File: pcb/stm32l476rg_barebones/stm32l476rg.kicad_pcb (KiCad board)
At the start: 4 copper layers, 50 x 38 mm, 49 parts, among them J1 Conn_01x04_UART, J2 Conn_01x04_I2C, J3 Conn_01x06_SPI, J4 SWD_Connector, J5 USB_B_Micro, J6 Screw_Terminal_01x02, Q1 AO3401A, SW1 SW_SPDT, U1 USBLC6-2SC6, U2 MP2359DJ-LF-Z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

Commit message: Pre barebones route
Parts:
- moved R8 3.26 mm to (143.3, 129.9), turned to 90 degrees
- moved D1 1.57 mm to (144.0, 114.2)
- moved U1 1.44 mm to (140.3, 113.8)
- moved R6 0.80 mm to (140.0, 129.9)
- moved R7 0.80 mm to (141.7, 129.9)
- moved Q1 0.55 mm to (143.2, 122.4)
- moved J6 0.35 mm to (149.2, 124.4)
- moved D3 0.30 mm to (147.5, 130.0)
- moved L2 0.27 mm to (133.2, 127.7)
- moved C7 0.25 mm to (137.1, 126.0)
- moved D2 0.25 mm to (133.7, 123.0)
- moved D4 0.14 mm to (147.5, 117.5)
- moved R11 0.14 mm to (147.5, 115.5)
- moved R10 0.10 mm to (147.5, 128.0)
- turned J5 to 180 degrees
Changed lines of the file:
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@@
   )
   (module Capacitor_SMD:C_0603_1608Metric (layer F.Cu)
-    (at 136.8 125.9 270)
+    (at 137.05 125.95 270)
     (descr "Capacitor SMD 0603 (1608 Metric), square (rectangular) end terminal, IPC_7351 nominal, (Body size source: IPC-SM-782 page 76, https://www.pcb-3d.com/wordpress/wp-content/uploads/ipc-sm-782a_amendment_1_and_2.pdf), generated with kicad-footprint-generator")
     (tags capacitor)
@@
   )
   (module Diode_SMD:D_SOD-123 (layer F.Cu)
-    (at 142.5 114.7 90)
+    (at 144 114.25 90)
     (descr SOD-123)
     (tags SOD-123)
@@
   )
   (module Diode_SMD:D_SOD-123 (layer F.Cu)
-    (at 133.4 123 180)
+    (at 133.65 123 180)
     (descr SOD-123)
     (tags SOD-123)
@@
   )
   (module LED_SMD:LED_0603_1608Metric (layer F.Cu)
-    (at 147.5 129.7 180)
+    (at 147.5 130 180)
     (descr "LED SMD 0603 (1608 Metric), square (rectangular) end terminal, IPC_7351 nominal, (Body size source: http://www.tortai-tech.com/upload/download/2011102023233369053.pdf), generated with kicad-footprint-generator")
     (tags LED)
@@
   )
   (module LED_SMD:LED_0603_1608Metric (layer F.Cu)
-    (at 147.6 117.4 180)
+    (at 147.5 117.5 180)
     (descr "LED SMD 0603 (1608 Metric), square (rectangular) end terminal, IPC_7351 nominal, (Body size source: http://www.tortai-tech.com/upload/download/2011102023233369053.pdf), generated with kicad-footprint-generator")
     (tags LED)
@@
   )
   (module Connector_USB:USB_Micro-B_Amphenol_10103594-0001LF_Horizontal (layer F.Cu)
-    (at 140 108.4)
+    (at 140 108.4 180)
     (descr "Micro USB Type B 10103594-0001LF, http://cdn.amphenol-icc.com/media/wysiwyg/files/drawing/10103594.pdf")
     (tags "USB USB_B USB_micro USB_OTG")
@@
       (effects (font (size 1 1) (thickness 0.15)))
     )
-    (pad 6 smd rect (at 2.725 0.185) (size 1.35 2) (layers F.Cu F.Paste F.Mask)
+    (pad 6 smd rect (at 2.725 0.185 180) (size 1.35 2) (layers F.Cu F.Paste F.Mask)
       (net 30 "Net-(J5-Pad6)"))
-    (pad 6 smd rect (at -2.755 0.185) (size 1.35 2) (layers F.Cu F.Paste F.Mask)
+    (pad 6 smd rect (at -2.755 0.185 180) (size 1.35 2) (layers F.Cu F.Paste F.Mask)
       (net 30 "Net-(J5-Pad6)"))
-    (pad 6 smd rect (at -2.975 -0.565) (size 1.825 0.7) (layers F.Cu F.Paste F.Mask)
+    (pad 6 smd rect (at -2.975 -0.565 180) (size 1.825 0.7) (layers F.Cu F.Paste F.Mask)
       (net 30 "Net-(J5-Pad6)"))
-    (pad 6 smd rect (at 2.975 -0.565) (size 1.825 0.7) (layers F.Cu F.Paste F.Mask)
+    (pad 6 smd rect (at 2.975 -0.565 180) (size 1.825 0.7) (layers F.Cu F.Paste F.Mask)
       (net 30 "Net-(J5-Pad6)"))
-    (pad 6 smd rect (at -2.875 -1.865) (size 2 1.5) (layers F.Cu F.Paste F.Mask)
+    (pad 6 smd rect (at -2.875 -1.865 180) (size 2 1.5) (layers F.Cu F.Paste F.Mask)
       (net 30 "Net-(J5-Pad6)"))
-    (pad 6 smd rect (at 2.875 -1.885) (size 2 1.5) (layers F.Cu F.Paste F.Mask)
+    (pad 6 smd rect (at 2.875 -1.885 180) (size 2 1.5) (layers F.Cu F.Paste F.Mask)
       (net 30 "Net-(J5-Pad6)"))
-    (pad 1 smd rect (at -1.325 -1.765 90) (size 1.65 0.4) (layers F.Cu F.Paste F.Mask)
+    (pad 1 smd rect (at -1.325 -1.765 270) (size 1.65 0.4) (layers F.Cu F.Paste F.Mask)
       (net 10 +5V))
-    (pad 2 smd rect (at -0.675 -1.765 90) (size 1.65 0.4) (layers F.Cu F.Paste F.Mask)
+    (pad 2 smd rect (at -0.675 -1.765 270) (size 1.65 0.4) (layers F.Cu F.Paste F.Mask)
       (net 31 USB_CONN_D-))
-    (pad 3 smd rect (at -0.025 -1.765 90) (size 1.65 0.4) (layers F.Cu F.Paste F.Mask)
+    (pad 3 smd rect (at -0.025 -1.765 270) (size 1.65 0.4) (layers F.Cu F.Paste F.Mask)
       (net 32 USB_CONN_D+))
-    (pad 4 smd rect (at 0.625 -1.765 90) (size 1.65 0.4) (layers F.Cu F.Paste F.Mask)
+    (pad 4 smd rect (at 0.625 -1.765 270) (size 1.65 0.4) (layers F.Cu F.Paste F.Mask)
       (net 33 "Net-(J5-Pad4)"))
-    (pad 5 smd rect (at 1.275 -1.765 90) (size 1.65 0.4) (layers F.Cu F.Paste F.Mask)
-      (net 1 GND))
-    (pad 6 thru_hole oval (at -2.445 -1.885 90) (size 1.5 1.1) (drill oval 1.05 0.65) (layers *.Cu *.Mask)
+    (pad 5 smd rect (at 1.275 -1.765 270) (size 1.65 0.4) (layers F.Cu F.Paste F.Mask)
+      (net 1 GND))
+    (pad 6 thru_hole oval (at -2.445 -1.885 270) (size 1.5 1.1) (drill oval 1.05 0.65) (layers *.Cu *.Mask)
       (net 30 "Net-(J5-Pad6)"))
-    (pad 6 thru_hole oval (at 2.395 -1.885 90) (size 1.5 1.1) (drill oval 1.05 0.65) (layers *.Cu *.Mask)
+    (pad 6 thru_hole oval (at 2.395 -1.885 270) (size 1.5 1.1) (drill oval 1.05 0.65) (layers *.Cu *.Mask)
       (net 30 "Net-(J5-Pad6)"))
-    (pad 6 thru_hole oval (at -2.755 1.115 90) (size 1.7 1.35) (drill oval 1.2 0.7) (layers *.Cu *.Mask)
+    (pad 6 thru_hole oval (at -2.755 1.115 270) (size 1.7 1.35) (drill oval 1.2 0.7) (layers *.Cu *.Mask)
       (net 30 "Net-(J5-Pad6)"))
-    (pad 6 thru_hole oval (at 2.705 1.115 90) (size 1.7 1.35) (drill oval 1.2 0.7) (layers *.Cu *.Mask)
+    (pad 6 thru_hole oval (at 2.705 1.115 270) (size 1.7 1.35) (drill oval 1.2 0.7) (layers *.Cu *.Mask)
       (net 30 "Net-(J5-Pad6)"))
-    (pad 6 smd rect (at -0.985 1.385 90) (size 2.5 1.43) (layers F.Cu F.Paste F.Mask)
+    (pad 6 smd rect (at -0.985 1.385 270) (size 2.5 1.43) (layers F.Cu F.Paste F.Mask)
       (net 30 "Net-(J5-Pad6)"))
-    (pad 6 smd rect (at 0.935 1.385 90) (size 2.5 1.43) (layers F.Cu F.Paste F.Mask)
+    (pad 6 smd rect (at 0.935 1.385 270) (size 2.5 1.43) (layers F.Cu F.Paste F.Mask)
       (net 30 "Net-(J5-Pad6)"))
     (model ${KISYS3DMOD}/Connector_USB.3dshapes/USB_Micro-B_Amphenol_10103594-0001LF_Horizontal.wrl
@@
   )
   (module TerminalBlock_Phoenix:TerminalBlock_Phoenix_PT-1,5-2-3.5-H_1x02_P3.50mm_Horizontal (layer F.Cu)
-    (at 149.6 124.4 90)
+    (at 149.25 124.4 90)
     (descr "Terminal Block Phoenix PT-1,5-2-3.5-H, 2 pins, pitch 3.5mm, size 7x7.6mm^2, drill diamater 1.2mm, pad diameter 2.4mm, see , script-generated using https://github.com/pointhi/kicad-footprint-generator/scripts/TerminalBlock_Phoenix")
     (tags "THT Terminal Block Phoenix PT-1,5-2-3.5-H pitch 3.5mm size 7x7.6mm^2 drill 1.2mm pad 2.4mm")
@@
   )
   (module Inductor_SMD:L_Sunlord_MWSA0518_5.4x5.2mm (layer F.Cu)
-    (at 132.9 127.6 270)
+    (at 133.15 127.7 270)
     (descr "Inductor, Sunlord, MWSA0518, 5.4mmx5.2mm")
     (tags "inductor Sunlord smd")
@@
   )
   (module Package_TO_SOT_SMD:SOT-23 (layer F.Cu)
-    (at 143.8 122.4 270)
+    (at 143.25 122.4 270)
     (descr "SOT-23, Standard")
     (tags SOT-23)
@@
   )
   (module Resistor_SMD:R_0603_1608Metric (layer F.Cu)
-    (at 140.8 129.9 90)
+    (at 140 129.95 90)
     (descr "Resistor SMD 0603 (1608 Metric), square (rectangular) end terminal, IPC_7351 nominal, (Body size source: IPC-SM-782 page 72, https://www.pcb-3d.com/wordpress/wp-content/uploads/ipc-sm-782a_amendment_1_and_2.pdf), generated with kicad-footprint-generator")
     (tags resistor)
@@
   )
   (module Resistor_SMD:R_0603_1608Metric (layer F.Cu)
-    (at 142.5 129.9 270)
+    (at 141.7 129.95 270)
     (descr "Resistor SMD 0603 (1608 Metric), square (rectangular) end terminal, IPC_7351 nominal, (Body size source: IPC-SM-782 page 72, https://www.pcb-3d.com/wordpress/wp-content/uploads/ipc-sm-782a_amendment_1_and_2.pdf), generated with kicad-footprint-generator")
     (tags resistor)
@@
   )
   (module Resistor_SMD:R_0603_1608Metric (layer F.Cu)
-    (at 142.5 133.1 270)
+    (at 143.35 129.95 90)
     (descr "Resistor SMD 0603 (1608 Metric), square (rectangular) end terminal, IPC_7351 nominal, (Body size source: IPC-SM-782 page 72, https://www.pcb-3d.com/wordpress/wp-content/uploads/ipc-sm-782a_amendment_1_and_2.pdf), generated with kicad-footprint-generator")
     (tags resistor)
@@
     (fp_line (start 1.48 -0.73) (end 1.48 0.73) (layer F.CrtYd) (width 0.05))
     (fp_line (start 1.48 0.73) (end -1.48 0.73) (layer F.CrtYd) (width 0.05))
-    (pad 2 smd roundrect (at 0.825 0 270) (size 0.8 0.95) (layers F.Cu F.Paste F.Mask) (roundrect_rratio 0.25)
-      (net 1 GND))
-    (pad 1 smd roundrect (at -0.825 0 270) (size 0.8 0.95) (layers F.Cu F.Paste F.Mask) (roundrect_rratio 0.25)
+    (pad 2 smd roundrect (at 0.825 0 90) (size 0.8 0.95) (layers F.Cu F.Paste F.Mask) (roundrect_rratio 0.25)
+      (net 1 GND))
+    (pad 1 smd roundrect (at -0.825 0 90) (size 0.8 0.95) (layers F.Cu F.Paste F.Mask) (roundrect_rratio 0.25)
       (net 38 "Net-(R7-Pad2)"))
     (model ${KISYS3DMOD}/Resistor_SMD.3dshapes/R_0603_1608Metric.wrl
@@
   )
   (module Resistor_SMD:R_0603_1608Metric (layer F.Cu)
-    (at 147.5 127.9 180)
+    (at 147.5 128 180)
     (descr "Resistor SMD 0603 (1608 Metric), square (rectangular) end terminal, IPC_7351 nominal, (Body size source: IPC-SM-782 page 72, https://www.pcb-3d.com/wordpress/wp-content/uploads/ipc-sm-782a_amendment_1_and_2.pdf), generated with kicad-footprint-generator")
     (tags resistor)
@@
   )
   (module Resistor_SMD:R_0603_1608Metric (layer F.Cu)
-    (at 147.6 115.6 180)
+    (at 147.5 115.5 180)
     (descr "Resistor SMD 0603 (1608 Metric), square (rectangular) end terminal, IPC_7351 nominal, (Body size source: IPC-SM-782 page 72, https://www.pcb-3d.com/wordpress/wp-content/uploads/ipc-sm-782a_amendment_1_and_2.pdf), generated with kicad-footprint-generator")
     (tags resistor)
@@
   )
   (module Package_TO_SOT_SMD:SOT-23-6 (layer F.Cu)
-    (at 139 114.3 270)
+    (at 140.35 113.8 270)
     (descr "6-pin SOT-23 package")
     (tags SOT-23-6)
@@
   )
   (module Package_TO_SOT_SMD:SOT-23-6 (layer F.Cu)
-    (at 139.9 126.3 90)
+    (at 139.9 126.35 90)
     (descr "6-pin SOT-23 package")
     (tags SOT-23-6)

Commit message: Traced barebones
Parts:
- moved D3 14.5 mm to (147.5, 115.5)
- moved D4 12.5 mm to (147.5, 130.0)
- moved R11 12.5 mm to (147.5, 128.0)
- moved R10 10.5 mm to (147.5, 117.5)
- moved C12 3.16 mm to (130.8, 132.3), turned to 0 degrees
- moved R3 2.63 mm to (126.5, 111.5), turned to 180 degrees
- moved J2 1.51 mm to (122.9, 109.0)
- moved C11 1.48 mm to (135.6, 132.3), turned to 180 degrees
- moved J5 1.40 mm to (140.0, 107.0)
- moved Q1 1.40 mm to (143.2, 121.0)
- moved J3 1.30 mm to (116.2, 136.0)
- moved J1 1.28 mm to (126.8, 136.0)
- moved R4 1.18 mm to (142.8, 124.5), turned to 270 degrees
- moved F1 0.50 mm to (138.9, 118.3)
- moved U1 0.30 mm to (140.3, 113.5)
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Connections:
- U3 pad 20: SPI1_CS1 -> Net-(U3-Pad20)
- U3 pad 24: Net-(U3-Pad24) -> SPI1_CS1
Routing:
- net GND: track 0.00 -> 66.3 mm, vias 0 -> 39
- net +3V3: track 0.00 -> 42.6 mm, vias 0 -> 21
- net LED_STATUS: track 0.00 -> 32.7 mm
- net NRST: track 0.00 -> 21.3 mm, vias 0 -> 2
- net BOOT0: track 0.00 -> 20.3 mm, vias 0 -> 2
- net USB_D-: track 0.00 -> 19.2 mm
- net USB_D+: track 0.00 -> 18.6 mm
- net SPI1_CS1: track 0.00 -> 16.4 mm
- net UART3_RX: track 0.00 -> 14.0 mm
- net SWIDO: track 0.00 -> 12.6 mm
- net SWO: track 0.00 -> 12.4 mm
- net HSE_IN: track 0.00 -> 11.9 mm
- net Net-(J5-Pad6): track 0.00 -> 11.5 mm
- net UART3_TX: track 0.00 -> 10.3 mm
- net +5V: track 0.00 -> 9.79 mm
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- added copper zone on In2.Cu, net +3V3
- added copper zone on In1.Cu, net GND

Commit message: Barebones connector fix
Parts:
- J4: footprint Connector_PinSocket_1.27mm:PinSocket_2x05_P1.27mm_Vertical_SMD -> Connector_PinHeader_1.27mm:PinHeader_2x05_P1.27mm_Vertical_SMD
- moved R3 1.10 mm to (125.4, 111.5)
- moved J4 0.10 mm to (131.8, 114.2), turned to 180 degrees
- moved SW1 0.10 mm to (130.5, 107.4)
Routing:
- net SWIDO: track 12.6 -> 8.69 mm
- net SWO: track 12.4 -> 9.46 mm
- net SWCLK: track 7.18 -> 4.87 mm
- net Net-(R3-Pad1): track 3.86 -> 5.28 mm
- net BOOT0: track 20.3 -> 19.2 mm
- net NRST: track 21.3 -> 20.7 mm
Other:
- board text added: "BOOT"
- board text added: "I2C"
- board text added: "JLCJLCJLCJLC"
- board text added: "PWR"
- board text added: "RUN"
- board text added: "SPI"
- board text added: "UART"
- board text added: "Willios"
- board text added: "v1"

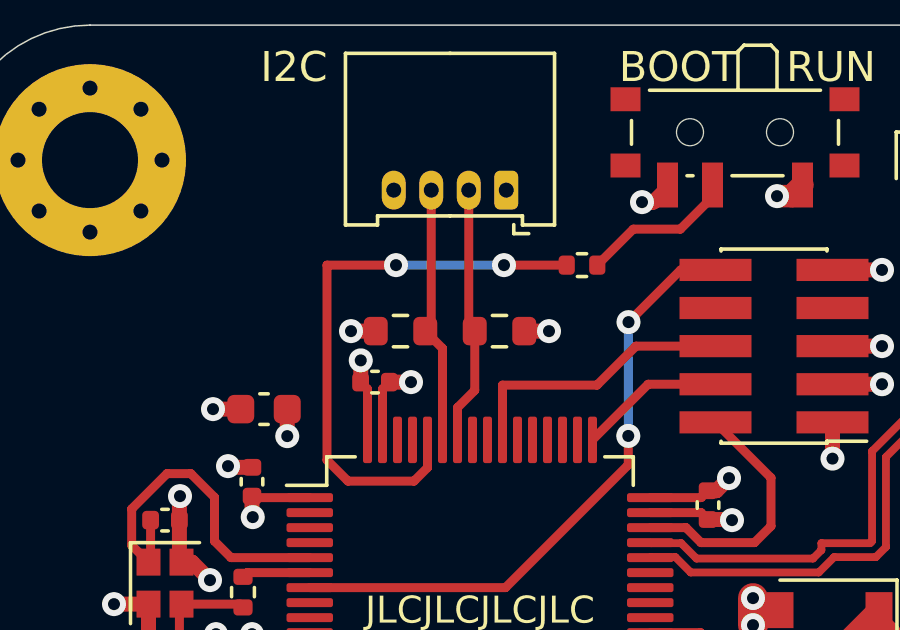
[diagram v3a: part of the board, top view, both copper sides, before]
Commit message: Changed pull up resistor size for i2c to get basic part
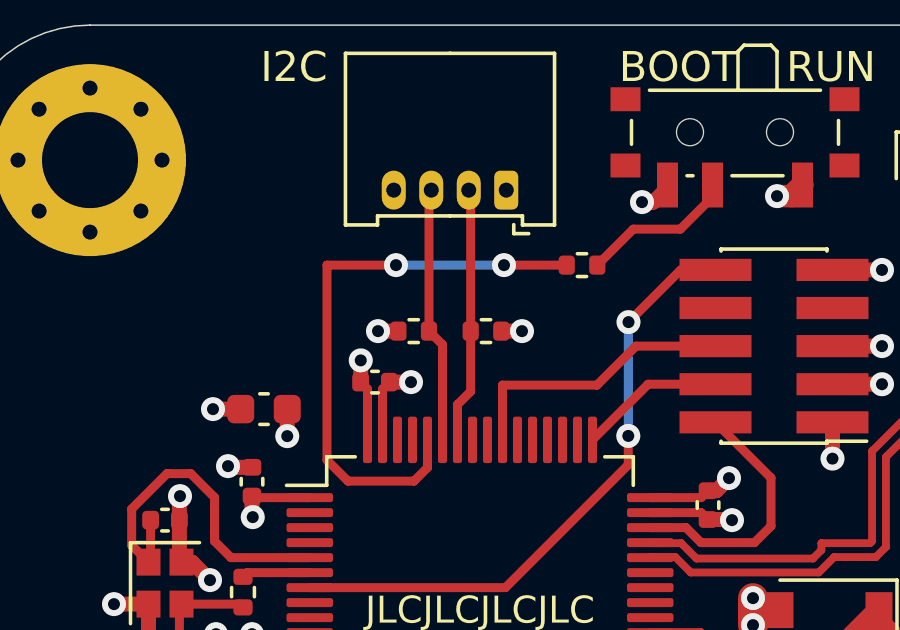
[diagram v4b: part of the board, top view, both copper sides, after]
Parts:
- R1, R2: footprint Resistor_SMD:R_0603_1608Metric -> Resistor_SMD:R_0402_1005Metric
- moved R1 0.45 mm to (122.2, 113.7)
- moved R2 0.44 mm to (119.8, 113.7)

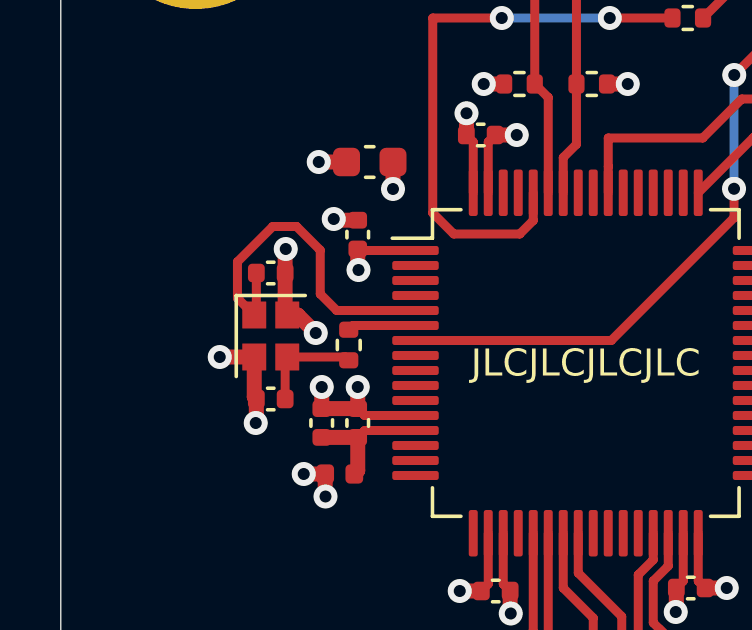
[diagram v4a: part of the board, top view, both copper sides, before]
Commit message: Resized crystal oscillator
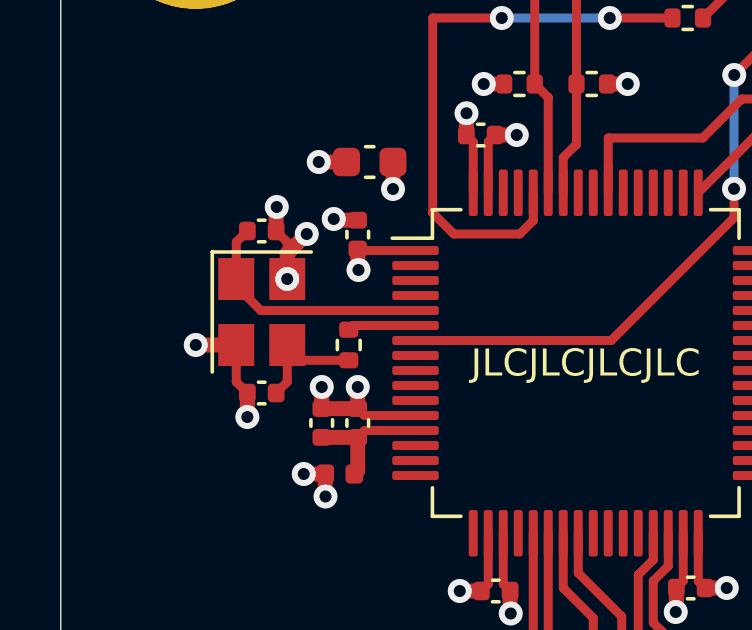
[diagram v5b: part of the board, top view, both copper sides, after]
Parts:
- Y1: value HSE_16MHz_X201616MLD4SI -> HSE_16MHz; footprint Crystal:Crystal_SMD_2016-4Pin_2.0x1.6mm -> Crystal:Crystal_SMD_3225-4Pin_3.2x2.5mm
- moved C13 1.43 mm to (111.2, 118.6)
- moved Y1 0.85 mm to (111.2, 121.3)
- moved C14 0.36 mm to (111.2, 124.0)
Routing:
- net HSE_IN: track 11.9 -> 8.30 mm
- net GND: track 65.8 -> 67.1 mm, vias 39 -> 40
- net Net-(C14-Pad2): track 3.52 -> 4.17 mm
